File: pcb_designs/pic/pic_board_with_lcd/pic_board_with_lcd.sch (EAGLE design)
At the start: 26 parts, among them IC1 PIC16f877a, IC2 7805TV

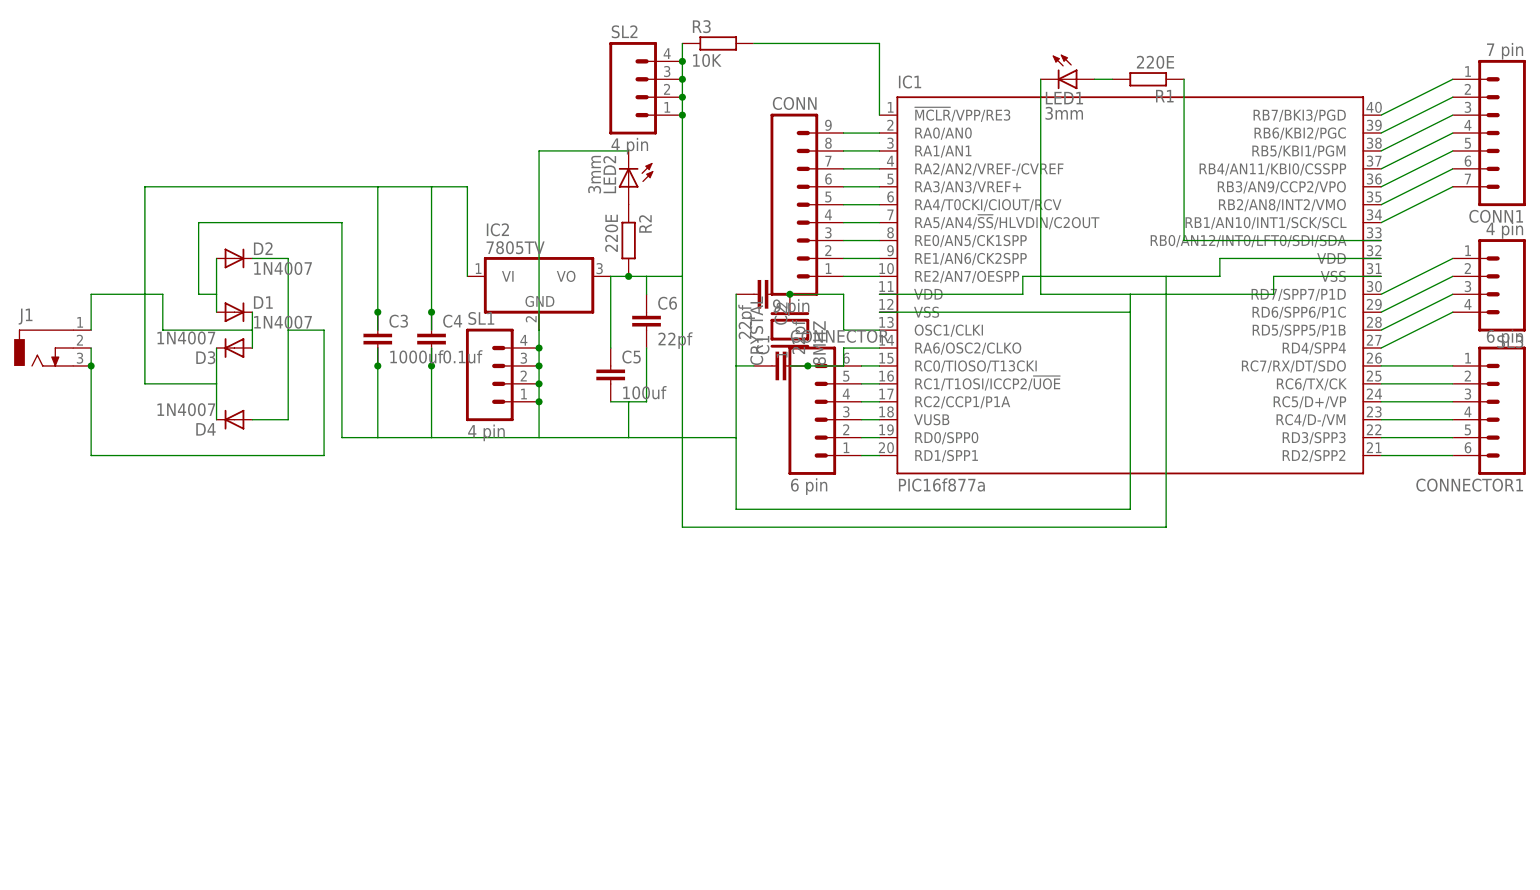
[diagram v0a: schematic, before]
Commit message: ADD PIC WITH LCD
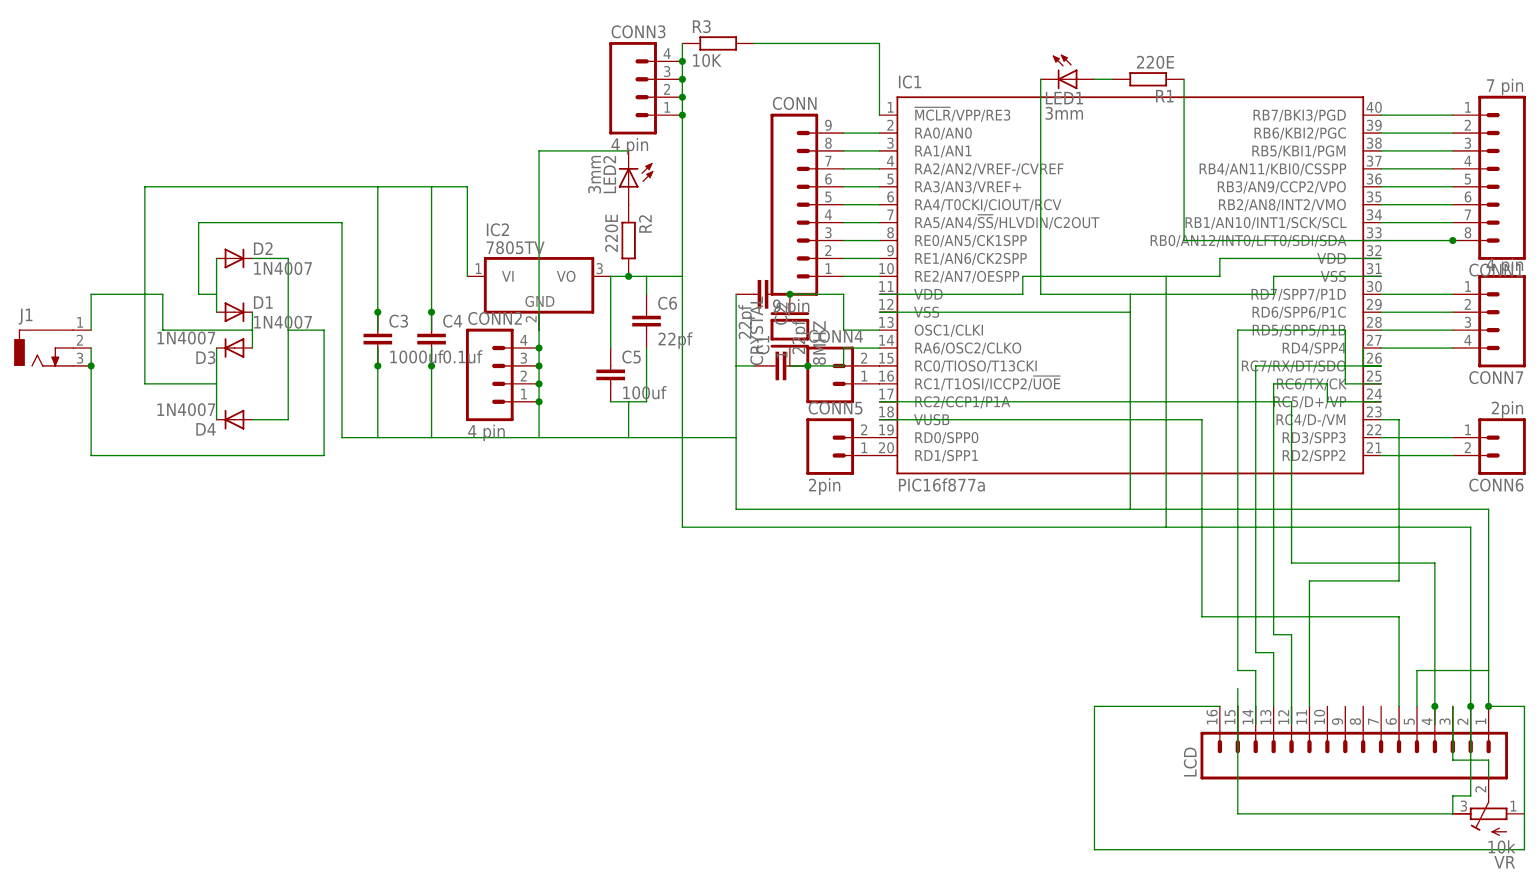
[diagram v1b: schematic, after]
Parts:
- removed CONNECTOR, CONNECTOR1: 6 pin, con-amp-quick:M06
- removed SL3: 4 pin, con-amp-quick:M04
- added CONN4: (no value), con-amp-quick:M02
- added CONN5, CONN6: 2pin, con-amp-quick:M02
- added CONN7: 4 pin, con-amp-quick:M04
- added LCD: (no value), con-amp-quick:M16
- added VR: 10k, resistor:R-TRIMM64P
- CONN1: device con-amp-quick:M07 -> con-amp-quick:M08
- renumbered SL1 to CONN2, SL2 to CONN3
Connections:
- new net N$46: IC1.VUSB, LCD.6
- net N$13: now also CONN5.1; no longer CONNECTOR.1
- net N$14: now also CONN5.2; no longer CONNECTOR.2
- net N$15: now also CONN4.1, IC1.RC1/T1OSI/ICCP2/!UOE; no longer CONNECTOR.3, IC1.VUSB
- net N$16: now also CONN4.2, IC1.RC0/TIOSO/T13CKI; no longer CONNECTOR.4, IC1.RC2/CCP1/P1A
- net N$17: now also IC1.RC2/CCP1/P1A, LCD.4; no longer CONNECTOR.5, IC1.RC1/T1OSI/ICCP2/!UOE
- net N$18: now also CONN6.1, IC1.RD3/SPP3; no longer CONNECTOR.6, IC1.RC0/TIOSO/T13CKI
- net N$26: now also CONN6.2, IC1.RD2/SPP2; no longer CONNECTOR1.1, IC1.RC7/RX/DT/SDO
- net N$27: now also CONN7.1, IC1.RD7/SPP7/P1D; no longer CONNECTOR1.2, IC1.RC6/TX/CK
- net N$28: now also CONN7.2, IC1.RD6/SPP6/P1C; no longer CONNECTOR1.3, IC1.RC5/D+/VP
- net N$29: now also CONN1.8
- net N$33: now also LCD.15, LCD.2, VR.A
- net N$35: now also LCD.1, LCD.16, LCD.5, VR.E
- net N$36: now also CONN7.3, IC1.RD5/SPP5/P1B; no longer CONNECTOR1.4, IC1.RC4/D-/VM
- net N$37: now also CONN7.4, IC1.RD4/SPP4; no longer CONNECTOR1.5, IC1.RD3/SPP3
- net N$38: now also IC1.RC4/D-/VM, LCD.11; no longer CONNECTOR1.6, IC1.RD2/SPP2
- net N$40: now also LCD.3, VR.S; no longer IC1.RD7/SPP7/P1D, SL3.1
- net N$41: now also IC1.RC5/D+/VP, LCD.12; no longer IC1.RD6/SPP6/P1C, SL3.2
- net N$42: now also IC1.RC6/TX/CK, LCD.13; no longer IC1.RD5/SPP5/P1B, SL3.3
- net N$43: now also IC1.RC7/RX/DT/SDO, LCD.14; no longer IC1.RD4/SPP4, SL3.4
